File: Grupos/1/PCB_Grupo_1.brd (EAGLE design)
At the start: 100 x 80 mm, 45 parts, among them T1 2N7002-7-F, T2 2N7002-7-F, U1 MAX3221ECPWR, U2 ST1S14PHR, U3 MAX31855KASA+T

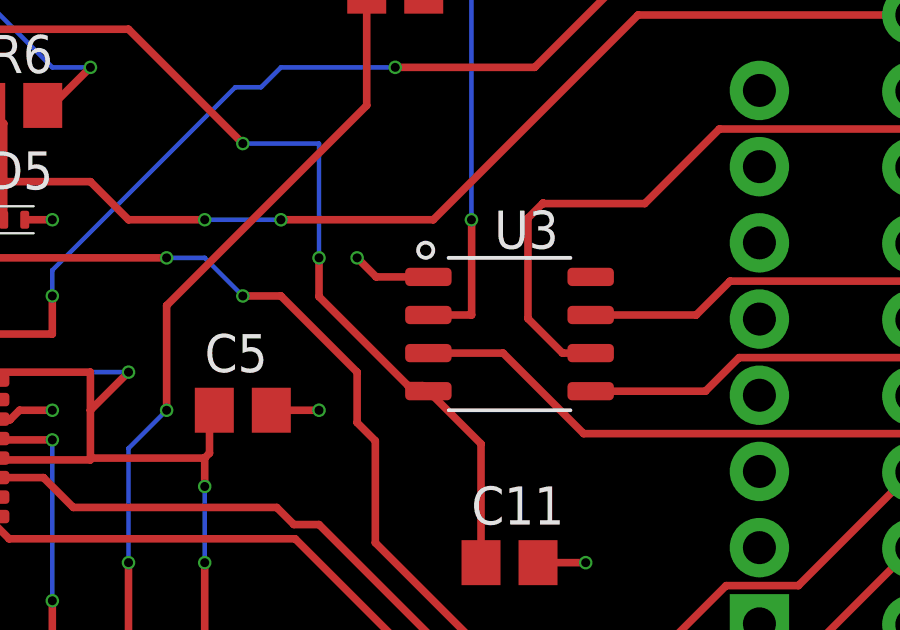
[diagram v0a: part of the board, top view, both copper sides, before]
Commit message: Se arregla error crítico en la fuente de poder
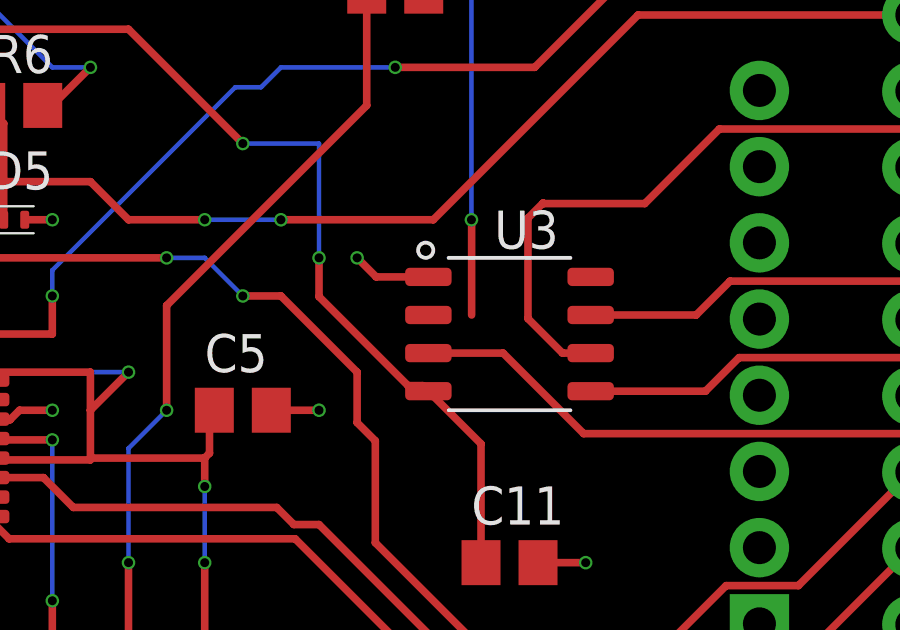
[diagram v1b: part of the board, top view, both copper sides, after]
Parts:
- R4: value 80.6 k -> 301K
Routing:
- net N$29: track 91.7 -> 90.2 mm
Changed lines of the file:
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@@
 <attribute name="VALUE" x="33.655" y="54.61" size="1.27" layer="27" rot="R180"/>
 </element>
-<element name="R4" library="rcl" library_urn="urn:adsk.eagle:library:334" package="R0805" package3d_urn="urn:adsk.eagle:package:23553/2" value="80.6 k" x="39.37" y="54.61" smashed="yes" rot="R180">
+<element name="R4" library="rcl" library_urn="urn:adsk.eagle:library:334" package="R0805" package3d_urn="urn:adsk.eagle:package:23553/2" value="301K" x="39.37" y="54.61" smashed="yes" rot="R180">
 <attribute name="NAME" x="40.175" y="57.12" size="1.27" layer="25" rot="R180"/>
-<attribute name="PART_NO" value="RC0805FR-0780K6L" x="21.59" y="143.51" size="1.778" layer="27" rot="R180" display="off"/>
+<attribute name="PARTNO" value="RC0805FR-07301KL" x="21.59" y="143.51" size="1.778" layer="27" rot="R180" display="off"/>
 <attribute name="POPULARITY" value="85" x="21.59" y="143.51" size="1.778" layer="27" rot="R180" display="off"/>
 <attribute name="SPICEPREFIX" value="R" x="21.59" y="143.51" size="1.778" layer="27" rot="R180" display="off"/>
@@
 <signal name="N$29">
 <contactref element="CT4" pad="5"/>
-<contactref element="U3" pad="2"/>
 <wire x1="92.71" y1="40.56" x2="88.9" y2="44.37" width="0.254" layer="1"/>
 <wire x1="88.9" y1="44.37" x2="88.9" y2="67.31" width="0.254" layer="1"/>
@@
 <wire x1="66.04" y1="48.26" x2="66.04" y2="29.21" width="0.1524" layer="16"/>
 <via x="66.04" y="29.21" extent="1-16" drill="0.3"/>
-<wire x1="66.0471375" y1="26.035" x2="64.6049" y2="26.035" width="0.254" layer="1"/>
 <wire x1="66.04" y1="29.21" x2="66.0471375" y2="29.2028625" width="0.254" layer="1"/>
 <wire x1="66.0471375" y1="29.2028625" x2="66.0471375" y2="26.035" width="0.254" layer="1"/>
+<contactref element="U3" pad="2"/>
+<wire x1="64.6049" y1="26.035" x2="66.0471375" y2="26.035" width="0" layer="19" extent="1-1"/>
 </signal>
 <signal name="N$30">
